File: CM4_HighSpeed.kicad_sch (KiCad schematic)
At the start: 13 parts, among them J10 690-019-298-412, J15 Conn_01x22_Female, J16 Conn_01x22_Female, J22 690-019-298-412, J4 Conn_01x22_Female, J5 Conn_01x22_Female, J6 THD-02-R, U12 RT9742SNGV

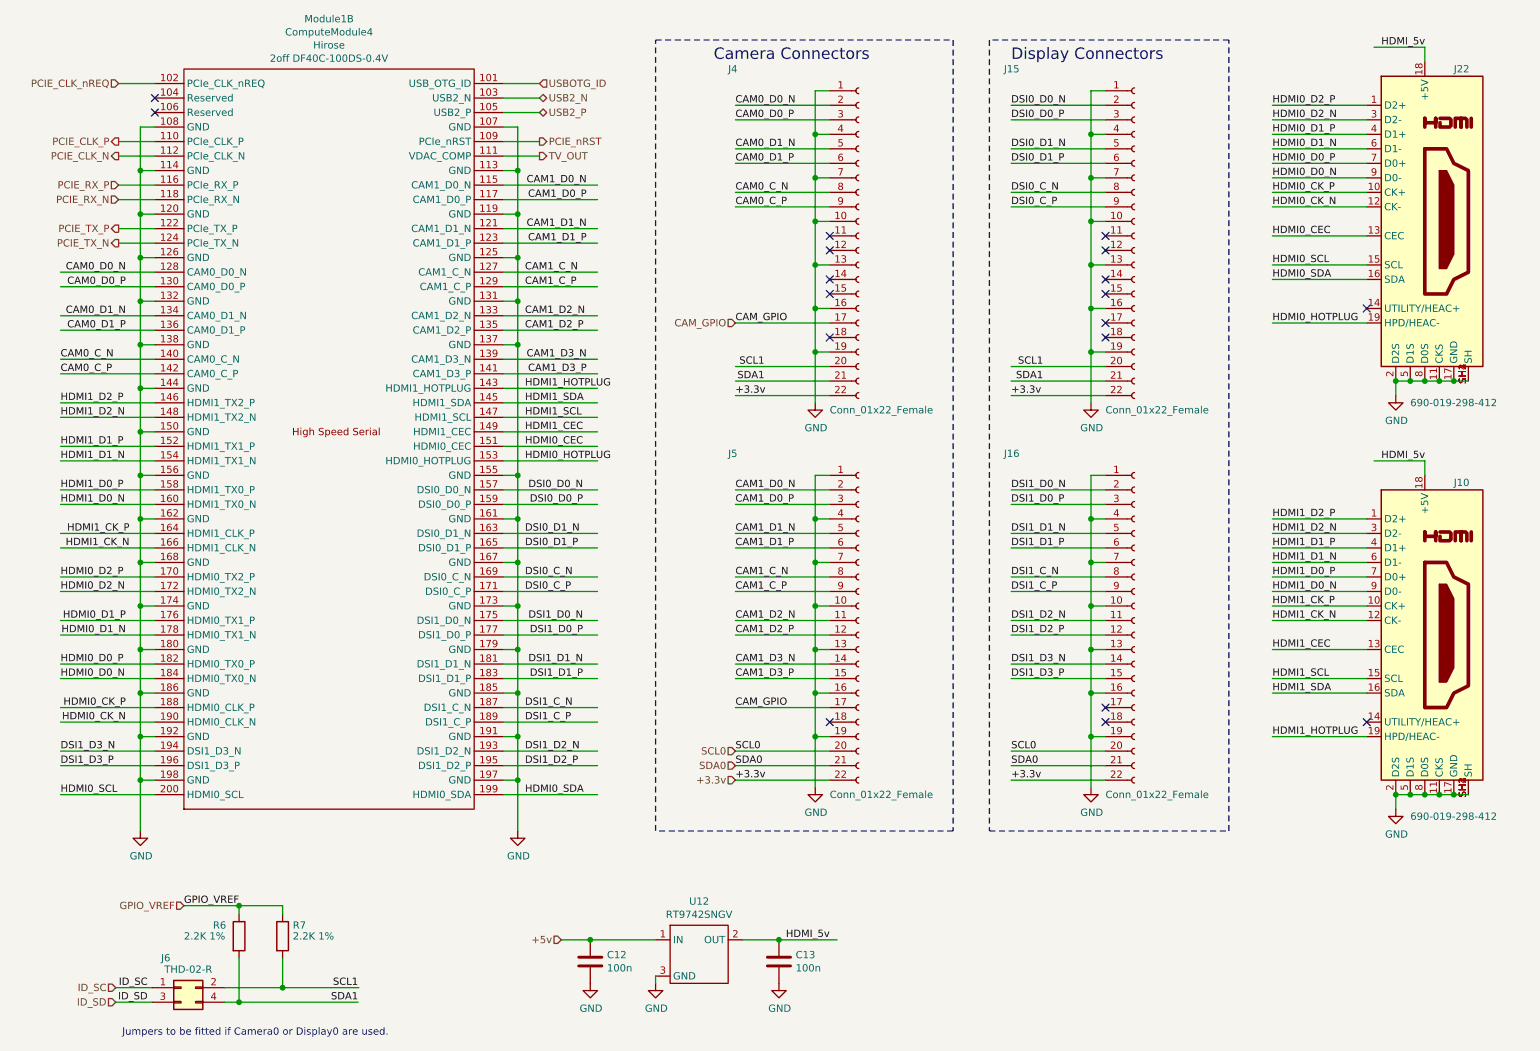
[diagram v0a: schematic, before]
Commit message: removed many unused parts
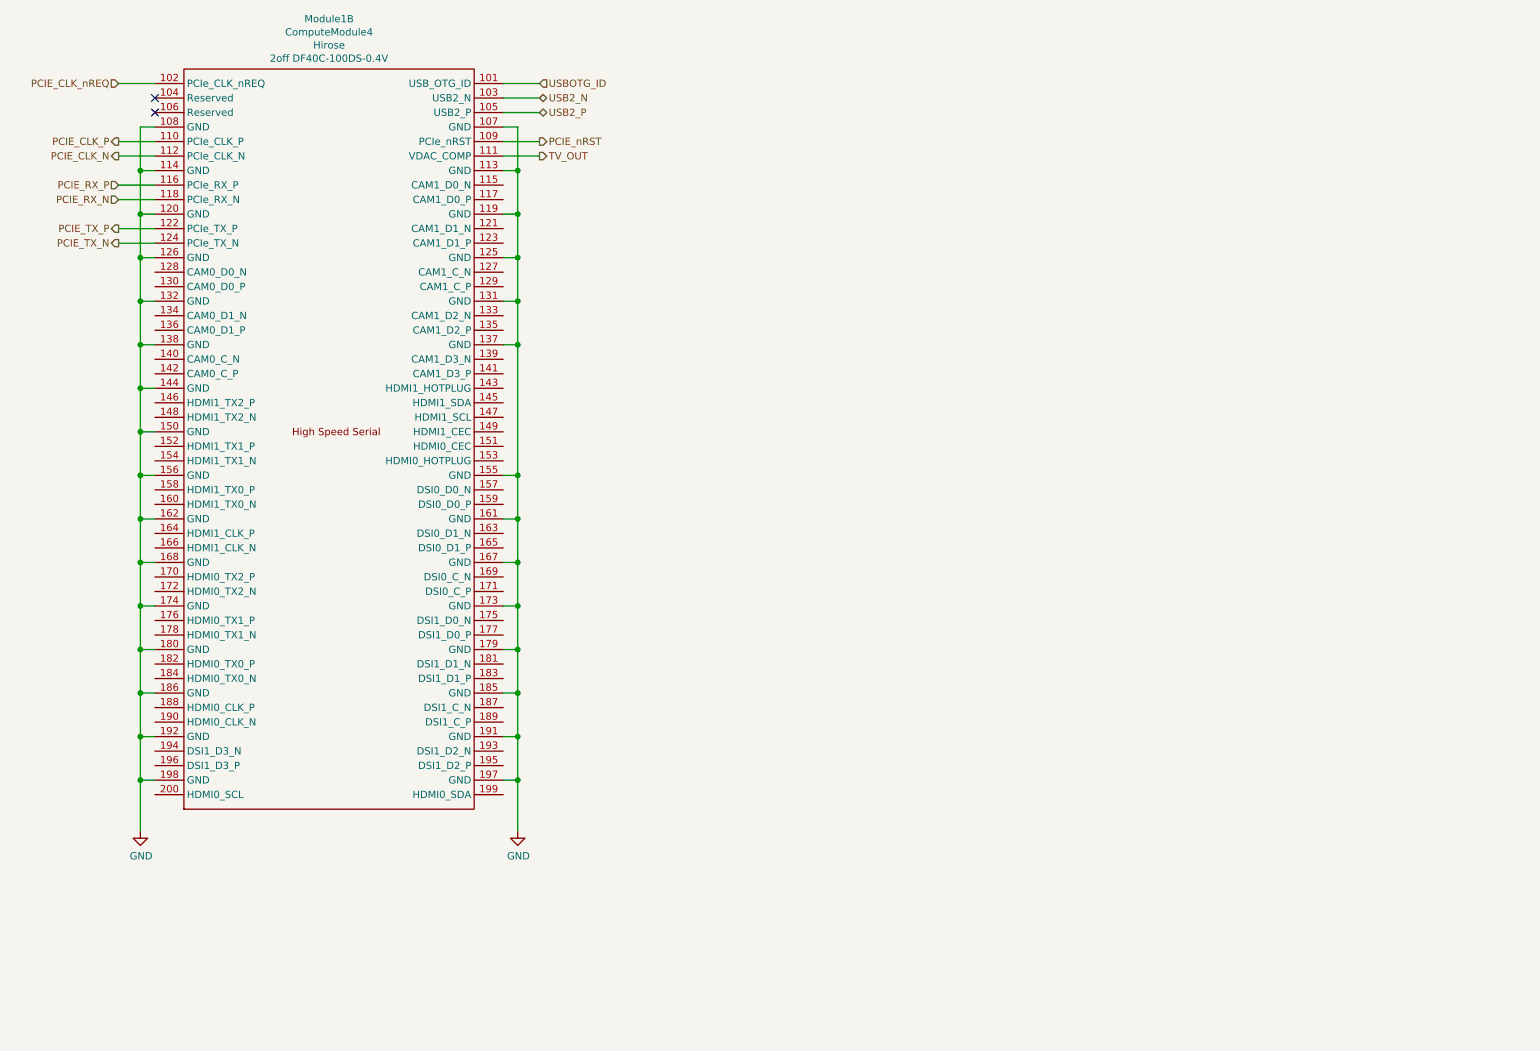
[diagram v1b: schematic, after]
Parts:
- removed C12, C13: 100n, Capacitor_SMD:C_0402_1005Metric, symbol Device:C
- removed J10, J22: 690-019-298-412, CM4IO:EDAC 690-019-298-412, symbol CM4IO:HDMI_A_1.4
- removed J15, J16, J4, J5: Conn_01x22_Female, Connector_FFC-FPC:Hirose_FH12-22S-0.5SH_1x22-1MP_P0.50mm_Horizontal, symbol Connector:Conn_01x22_Female
- removed J6: THD-02-R, Connector_PinHeader_2.54mm:PinHeader_2x02_P2.54mm_Vertical, symbol Connector_Generic:Conn_02x02_Odd_Even
- removed R6, R7: 2.2K 1%, Resistor_SMD:R_0402_1005Metric, symbol Device:R
- removed U12: RT9742SNGV, Package_TO_SOT_SMD:SOT-23, symbol CM4IO:RT9742SNGV
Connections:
- net CAM0_C_N: no longer names the net of Module1.140 (CAM0_C_N)
- net CAM0_C_P: no longer names the net of Module1.142 (CAM0_C_P)
- net CAM0_D0_N: no longer names the net of Module1.128 (CAM0_D0_N)
- net CAM0_D0_P: no longer names the net of Module1.130 (CAM0_D0_P)
- net CAM0_D1_N: no longer names the net of Module1.134 (CAM0_D1_N)
- net CAM0_D1_P: no longer names the net of Module1.136 (CAM0_D1_P)
- net CAM1_C_N: no longer names the net of Module1.127 (CAM1_C_N)
- net CAM1_C_P: no longer names the net of Module1.129 (CAM1_C_P)
- net CAM1_D0_N: no longer names the net of Module1.115 (CAM1_D0_N)
- net CAM1_D0_P: no longer names the net of Module1.117 (CAM1_D0_P)
- net CAM1_D1_N: no longer names the net of Module1.121 (CAM1_D1_N)
- net CAM1_D1_P: no longer names the net of Module1.123 (CAM1_D1_P)
- net CAM1_D2_N: no longer names the net of Module1.133 (CAM1_D2_N)
- net CAM1_D2_P: no longer names the net of Module1.135 (CAM1_D2_P)
- net CAM1_D3_N: no longer names the net of Module1.139 (CAM1_D3_N)
- net CAM1_D3_P: no longer names the net of Module1.141 (CAM1_D3_P)
- net DSI0_C_N: no longer names the net of Module1.169 (DSI0_C_N)
- net DSI0_C_P: no longer names the net of Module1.171 (DSI0_C_P)
- net DSI0_D0_N: no longer names the net of Module1.157 (DSI0_D0_N)
- net DSI0_D0_P: no longer names the net of Module1.159 (DSI0_D0_P)
- net DSI0_D1_N: no longer names the net of Module1.163 (DSI0_D1_N)
- net DSI0_D1_P: no longer names the net of Module1.165 (DSI0_D1_P)
- net DSI1_C_N: no longer names the net of Module1.187 (DSI1_C_N)
- net DSI1_C_P: no longer names the net of Module1.189 (DSI1_C_P)
- net DSI1_D0_N: no longer names the net of Module1.175 (DSI1_D0_N)
- net DSI1_D0_P: no longer names the net of Module1.177 (DSI1_D0_P)
- net DSI1_D1_N: no longer names the net of Module1.181 (DSI1_D1_N)
- net DSI1_D1_P: no longer names the net of Module1.183 (DSI1_D1_P)
- net DSI1_D2_N: no longer names the net of Module1.193 (DSI1_D2_N)
- net DSI1_D2_P: no longer names the net of Module1.195 (DSI1_D2_P)
- net DSI1_D3_N: no longer names the net of Module1.194 (DSI1_D3_N)
- net DSI1_D3_P: no longer names the net of Module1.196 (DSI1_D3_P)
- net HDMI0_CEC: no longer names the net of Module1.151 (HDMI0_CEC)
- net HDMI0_CK_N: no longer names the net of Module1.190 (HDMI0_CLK_N)
- net HDMI0_CK_P: no longer names the net of Module1.188 (HDMI0_CLK_P)
- net HDMI0_D0_N: no longer names the net of Module1.184 (HDMI0_TX0_N)
- net HDMI0_D0_P: no longer names the net of Module1.182 (HDMI0_TX0_P)
- net HDMI0_D1_N: no longer names the net of Module1.178 (HDMI0_TX1_N)
- net HDMI0_D1_P: no longer names the net of Module1.176 (HDMI0_TX1_P)
- net HDMI0_D2_N: no longer names the net of Module1.172 (HDMI0_TX2_N)
- net HDMI0_D2_P: no longer names the net of Module1.170 (HDMI0_TX2_P)
- net HDMI0_HOTPLUG: no longer names the net of Module1.153 (HDMI0_HOTPLUG)
- net HDMI0_SCL: no longer names the net of Module1.200 (HDMI0_SCL)
- net HDMI0_SDA: no longer names the net of Module1.199 (HDMI0_SDA)
- net HDMI1_CEC: no longer names the net of Module1.149 (HDMI1_CEC)
- net HDMI1_CK_N: no longer names the net of Module1.166 (HDMI1_CLK_N)
- net HDMI1_CK_P: no longer names the net of Module1.164 (HDMI1_CLK_P)
- net HDMI1_D0_N: no longer names the net of Module1.160 (HDMI1_TX0_N)
- net HDMI1_D0_P: no longer names the net of Module1.158 (HDMI1_TX0_P)
- net HDMI1_D1_N: no longer names the net of Module1.154 (HDMI1_TX1_N)
- net HDMI1_D1_P: no longer names the net of Module1.152 (HDMI1_TX1_P)
- net HDMI1_D2_N: no longer names the net of Module1.148 (HDMI1_TX2_N)
- net HDMI1_D2_P: no longer names the net of Module1.146 (HDMI1_TX2_P)
- net HDMI1_HOTPLUG: no longer names the net of Module1.143 (HDMI1_HOTPLUG)
- net HDMI1_SCL: no longer names the net of Module1.147 (HDMI1_SCL)
- net HDMI1_SDA: no longer names the net of Module1.145 (HDMI1_SDA)
- no-connect marks 18 -> 2
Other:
- note removed: "Camera Connectors"
- note removed: "Display Connectors"
- note removed: "Jumpers to be fitted if Camera0 or Display0 are used."
- company: © 2020-2022 Raspberry Pi Ltd (formerly Raspberry Pi (Trading) Ltd.) -> (none)
- title: Compute Module 4 IO Board - CM4 - Highspeed -> bticart - CM4 - Highspeed

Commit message: schematic cleanup
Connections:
- net PCIE_CLK_nREQ: no longer names the net of Module1.102 (PCIe_CLK_nREQ)
- net TV_OUT: no longer names the net of Module1.111 (VDAC_COMP)
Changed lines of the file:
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@@
-    (stroke (width 0) (type solid) (color 0 0 0 0))
-  )
-  (wire (pts (xy 35.56 26.67) (xy 41.91 26.67))
     (stroke (width 0) (type solid) (color 0 0 0 0))
   )
@@
     (stroke (width 0) (type solid) (color 0 0 0 0))
   )
-  (wire (pts (xy 102.87 39.37) (xy 109.22 39.37))
-    (stroke (width 0) (type solid) (color 0 0 0 0))
-  )
   (hierarchical_label "PCIE_RX_P" (shape input) (at 35.56 44.45 180)
     (effects (font (size 1.27 1.27)) (justify right))
-  )
-  (hierarchical_label "TV_OUT" (shape output) (at 109.22 39.37 0)
-    (effects (font (size 1.27 1.27)) (justify left))
   )
   (hierarchical_label "PCIE_CLK_N" (shape output) (at 35.56 39.37 180)
@@
     (effects (font (size 1.27 1.27)) (justify right))
   )
-  (hierarchical_label "PCIE_CLK_nREQ" (shape input) (at 35.56 26.67 180)
-    (effects (font (size 1.27 1.27)) (justify right))
-  )
